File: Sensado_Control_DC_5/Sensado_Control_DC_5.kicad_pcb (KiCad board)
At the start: 2 copper layers, 100 x 100 mm, 100 parts, among them J1 Jumper, J2 Jumper, J3 Jumper, P1 R_FUENTE_CON, P10 GPIO, P2 I_+, P3 I_-, P4 POWER, P5 RS-232, P6 I2C, P7 SPI, P8 GND_REG, P9 RESET, Q1 NMOS, Q10 PMOS, Q11 NMOS, Q12 NMOS, Q13 NMOS, Q14 PMOS, Q15 PMOS, Q16 PMOS, Q2 NMOS, Q3 NMOS, Q4 NMOS, Q5 NMOS, Q6 PMOS, Q7 PMOS, Q8 PMOS, Q9 PMOS, U1 Atmega328PA, U2 ACS_712, U3 LD1117S50TR_FINAL, Y1 XRCHA_16M

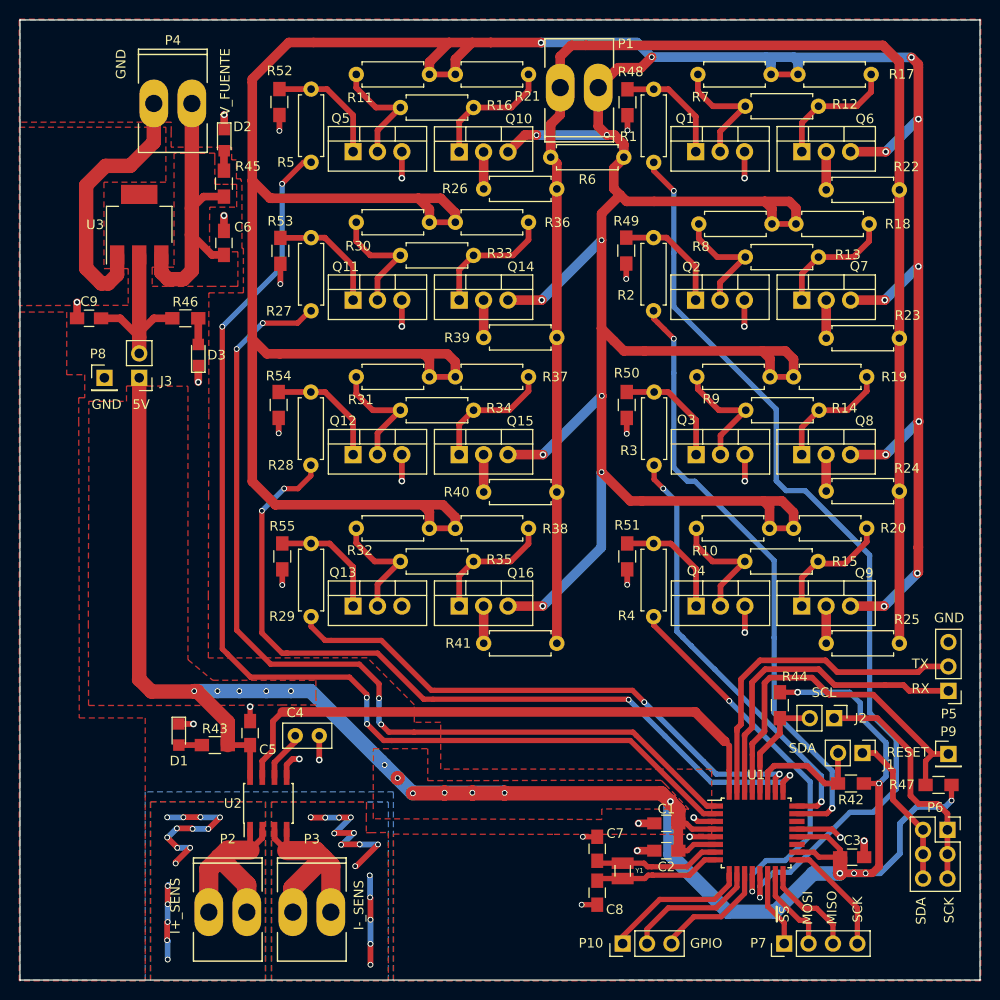
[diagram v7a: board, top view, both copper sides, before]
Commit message: Version PCB con tornillos incluidos
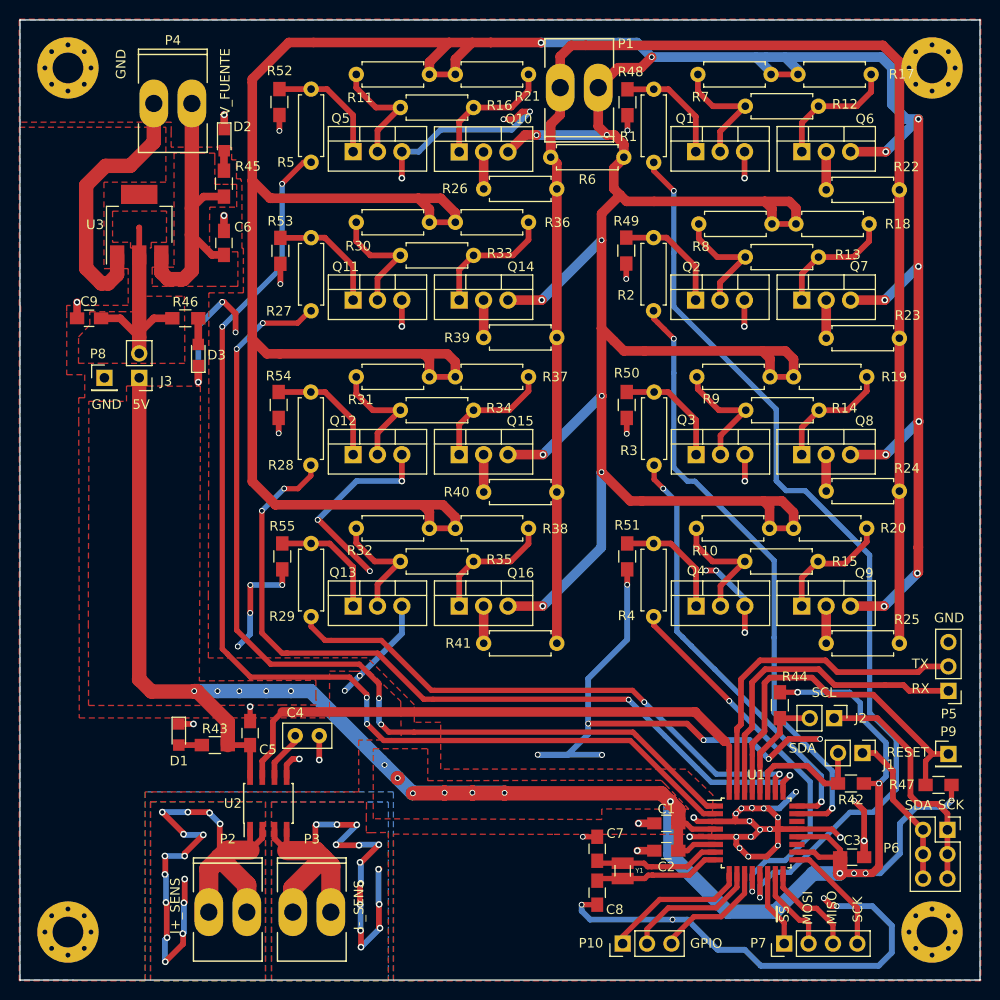
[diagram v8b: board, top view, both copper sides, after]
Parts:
- added P11: TOR_4, Mounting_Holes:MountingHole_3.2mm_M3_Pad_Via, F.Cu at (175.0, 145.0)
- added P12: TOR_2, Mounting_Holes:MountingHole_3.2mm_M3_Pad_Via, F.Cu at (175.0, 55.0)
- added P13: TOR_1, Mounting_Holes:MountingHole_3.2mm_M3_Pad_Via, F.Cu at (85.0, 55.0)
- added P14: TOR_3, Mounting_Holes:MountingHole_3.2mm_M3_Pad_Via, F.Cu at (85.0, 145.0)
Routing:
- net /GND: track 93.8 -> 312.5 mm, vias 31 -> 68
- net (no net): track 51.9 -> 0.00 mm, vias 31 -> 0
- net /I_SENS+: track 21.3 -> 62.5 mm, vias 0 -> 15
- net /I_SENS-: track 22.0 -> 57.3 mm, vias 0 -> 14
- net Net-(C9-Pad2): track 19.6 -> 22.4 mm
- net /VOUT: track 495.5 -> 495.2 mm, vias 19 -> 18
- added copper zone on F.Cu, net Net-(C9-Pad2)
- removed copper zone on F.Cu, net (none)
